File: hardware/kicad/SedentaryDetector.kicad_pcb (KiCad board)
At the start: 2 copper layers, 100 x 80 mm, 2 parts, among them J1 ESP32_2x15, J2 MPU6050_1x8

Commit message: feat(hardware): commit all hardware files for 100x80mm board
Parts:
- moved J2 47.7 mm to (149.5, 102.9)
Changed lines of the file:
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@@
 	(footprint ""
 		(layer "F.Cu")
-		(at 186.5 133)
+		(at 149.5 102.89)
 		(property "Reference" "J2"
 			(at 0 0 0)
@@
 		)
 		(property "Value" "MPU6050_1x8"
-			(at 0 0 0)
+			(at 6 3.38 0)
 			(layer "F.Fab")
 			(effects
@@
 		)
 		(property "Value" "ESP32_2x15"
-			(at 0 0 0)
+			(at 11 35.5 0)
 			(layer "F.Fab")
 			(effects
@@
 	)
 	(gr_text "J2-P8"
-		(at 188.5 115.22 0)
+		(at 151.5 85.34 0)
 		(layer "F.SilkS")
 		(effects
@@
 	)
 	(gr_text "J2-P7"
-		(at 188.5 117.76 0)
+		(at 151.5 87.88 0)
 		(layer "F.SilkS")
 		(effects
@@
 	)
 	(gr_text "J2-P6"
-		(at 188.5 120.3 0)
+		(at 151.5 90.42 0)
 		(layer "F.SilkS")
 		(effects
@@
 	)
 	(gr_text "J2-P5"
-		(at 188.5 122.84 0)
+		(at 151.5 92.96 0)
 		(layer "F.SilkS")
 		(effects
@@
 	)
 	(gr_text "J2-P4"
-		(at 188.5 125.38 0)
+		(at 151.5 95.5 0)
 		(layer "F.SilkS")
 		(effects
@@
 	)
 	(gr_text "J2-P3"
-		(at 188.5 127.92 0)
+		(at 151.5 98.04 0)
 		(layer "F.SilkS")
 		(effects
@@
 	)
 	(gr_text "J2-P2"
-		(at 188.5 130.46 0)
+		(at 151.5 100.58 0)
 		(layer "F.SilkS")
 		(effects
@@
 	)
 	(gr_text "J2-P1"
-		(at 188.5 133 0)
-		(layer "F.SilkS")
-		(effects
+		(at 151.5 103.12 0)
+		(layer "F.SilkS")
+		(effects

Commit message: chore: update PCB and scripts
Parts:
- moved J2 1.50 mm to (148.0, 103.0)
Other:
- board outline removed
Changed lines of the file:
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@@
 		(capping no)
 		(filling no)
+		(grid_origin 135.5 145)
 		(pcbplotparams
 			(layerselection 0x00000000_00000000_55555555_5755f5ff)
@@
 	(footprint ""
 		(layer "F.Cu")
-		(at 149.5 102.89)
+		(at 148 103)
 		(property "Reference" "J2"
 			(at 0 0 0)
@@
 		(embedded_fonts no)
 	)
-	(gr_line
-		(start 98.5 65)
-		(end 198.5 65)
-		(stroke
-			(width 0.1)
-			(type default)
-		)
-		(layer "Edge.Cuts")
-	)
-	(gr_line
-		(start 98.5 145)
-		(end 98.5 65)
-		(stroke
-			(width 0.1)
-			(type default)
-		)
-		(layer "Edge.Cuts")
-	)
-	(gr_line
-		(start 198.5 65)
-		(end 198.5 145)
-		(stroke
-			(width 0.1)
-			(type default)
-		)
-		(layer "Edge.Cuts")
-	)
-	(gr_line
-		(start 198.5 145)
-		(end 98.5 145)
-		(stroke
-			(width 0.1)
-			(type default)
-		)
-		(layer "Edge.Cuts")
-	)
 	(gr_text "L-P1"

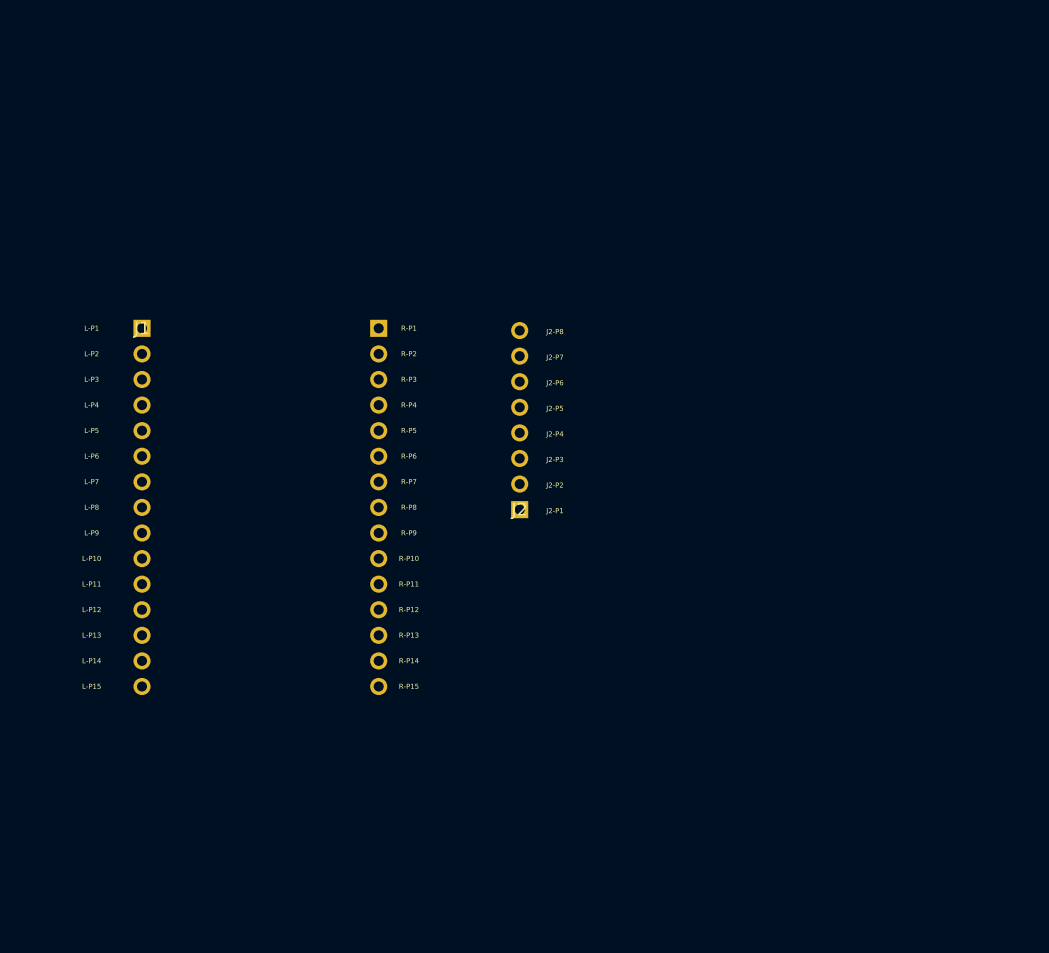
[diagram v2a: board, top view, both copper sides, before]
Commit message: fix(hardware): add missing Edge.Cuts board outline (100x80mm)
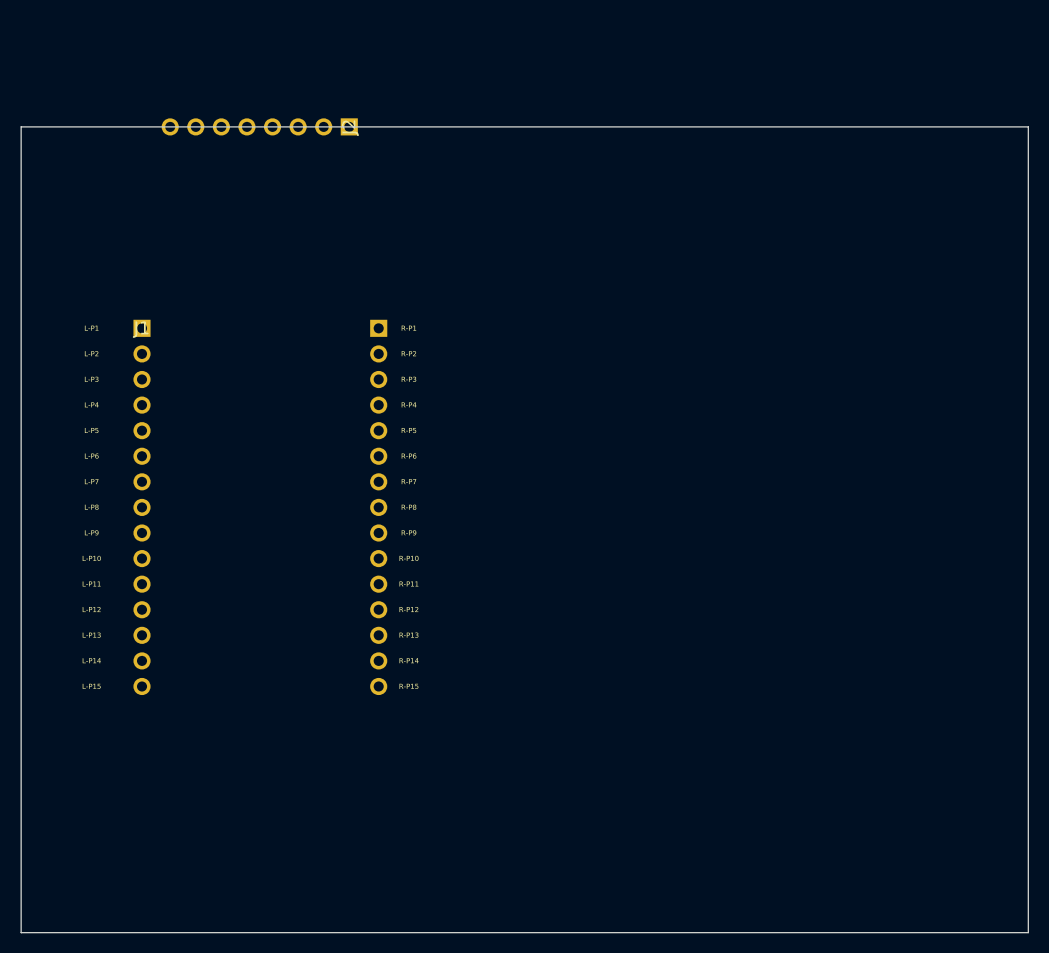
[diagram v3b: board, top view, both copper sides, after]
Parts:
- moved J2 41.6 mm to (131.1, 65.0), turned to 90 degrees
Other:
- board outline added: 100 x 80 mm
- board text removed: "J2-P1"
- board text removed: "J2-P2"
- board text removed: "J2-P3"
- board text removed: "J2-P4"
- board text removed: "J2-P5"
- board text removed: "J2-P6"
- board text removed: "J2-P7"
- board text removed: "J2-P8"
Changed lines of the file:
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@@
 	(footprint ""
 		(layer "F.Cu")
-		(at 148 103)
+		(at 131.08 65 90)
 		(property "Reference" "J2"
-			(at 0 0 0)
+			(at 0 0 90)
 			(layer "F.SilkS")
 			(effects
@@
 		)
 		(property "Value" "MPU6050_1x8"
-			(at 6 3.38 0)
+			(at 5.42 -8.5 0)
 			(layer "F.Fab")
 			(effects
@@
 		)
 		(property "Datasheet" ""
-			(at 0 0 0)
+			(at 0 0 90)
 			(layer "F.Fab")
 			(hide yes)
@@
 		)
 		(property "Description" ""
-			(at 0 0 0)
+			(at 0 0 90)
 			(layer "F.Fab")
 			(hide yes)
@@
 		(duplicate_pad_numbers_are_jumpers no)
 		(pad "1" thru_hole rect
-			(at 0 0)
+			(at 0 0 90)
 			(size 1.7 1.7)
 			(drill 1)
@@
 		)
 		(pad "2" thru_hole circle
-			(at 0 -2.54)
+			(at 0 -2.54 90)
 			(size 1.7 1.7)
 			(drill 1)
@@
 		)
 		(pad "3" thru_hole circle
-			(at 0 -5.08)
+			(at 0 -5.08 90)
 			(size 1.7 1.7)
 			(drill 1)
@@
 		)
 		(pad "4" thru_hole circle
-			(at 0 -7.62)
+			(at 0 -7.62 90)
 			(size 1.7 1.7)
 			(drill 1)
@@
 		)
 		(pad "5" thru_hole circle
-			(at 0 -10.16)
+			(at 0 -10.16 90)
 			(size 1.7 1.7)
 			(drill 1)
@@
 		)
 		(pad "6" thru_hole circle
-			(at 0 -12.7)
+			(at 0 -12.7 90)
 			(size 1.7 1.7)
 			(drill 1)
@@
 		)
 		(pad "7" thru_hole circle
-			(at 0 -15.24)
+			(at 0 -15.24 90)
 			(size 1.7 1.7)
 			(drill 1)
@@
 		)
 		(pad "8" thru_hole circle
-			(at 0 -17.78)
+			(at 0 -17.78 90)
 			(size 1.7 1.7)
 			(drill 1)
@@
 		(embedded_fonts no)
 	)
+	(gr_line
+		(start 98.5 65)
+		(end 198.5 65)
+		(stroke
+			(width 0.1)
+			(type default)
+		)
+		(layer "Edge.Cuts")
+	)
+	(gr_line
+		(start 98.5 145)
+		(end 98.5 65)
+		(stroke
+			(width 0.1)
+			(type default)
+		)
+		(layer "Edge.Cuts")
+	)
+	(gr_line
+		(start 198.5 65)
+		(end 198.5 145)
+		(stroke
+			(width 0.1)
+			(type default)
+		)
+		(layer "Edge.Cuts")
+	)
+	(gr_line
+		(start 198.5 145)
+		(end 98.5 145)
+		(stroke
+			(width 0.1)
+			(type default)
+		)
+		(layer "Edge.Cuts")
+	)
 	(gr_text "L-P1"
 		(at 105.5 85 0)
@@
 		(layer "F.SilkS")
 		(effects
-			(font
-				(size 0.5 0.5)
-				(thickness 0.15)
-			)
-		)
-	)
-	(gr_text "J2-P8"
-		(at 151.5 85.34 0)
-		(layer "F.SilkS")
-		(effects
-			(font
-				(size 0.5 0.5)
-				(thickness 0.15)
-			)
-		)
-	)
-	(gr_text "J2-P7"
-		(at 151.5 87.88 0)
-		(layer "F.SilkS")
-		(effects
-			(font
-				(size 0.5 0.5)
-				(thickness 0.15)
-			)
-		)
-	)
-	(gr_text "J2-P6"
-		(at 151.5 90.42 0)
-		(layer "F.SilkS")
-		(effects
-			(font
-				(size 0.5 0.5)
-				(thickness 0.15)
-			)
-		)
-	)
-	(gr_text "J2-P5"
-		(at 151.5 92.96 0)
-		(layer "F.SilkS")
-		(effects
-			(font
-				(size 0.5 0.5)
-				(thickness 0.15)
-			)
-		)
-	)
-	(gr_text "J2-P4"
-		(at 151.5 95.5 0)
-		(layer "F.SilkS")
-		(effects
-			(font
-				(size 0.5 0.5)
-				(thickness 0.15)
-			)
-		)
-	)
-	(gr_text "J2-P3"
-		(at 151.5 98.04 0)
-		(layer "F.SilkS")
-		(effects
-			(font
-				(size 0.5 0.5)
-				(thickness 0.15)
-			)
-		)
-	)
-	(gr_text "J2-P2"
-		(at 151.5 100.58 0)
-		(layer "F.SilkS")
-		(effects
-			(font
-				(size 0.5 0.5)
-				(thickness 0.15)
-			)
-		)
-	)
-	(gr_text "J2-P1"
-		(at 151.5 103.12 0)
-		(layer "F.SilkS")
-		(effects

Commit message: docs: add control circuit wiring table (ESP32 ↔ MPU6050)
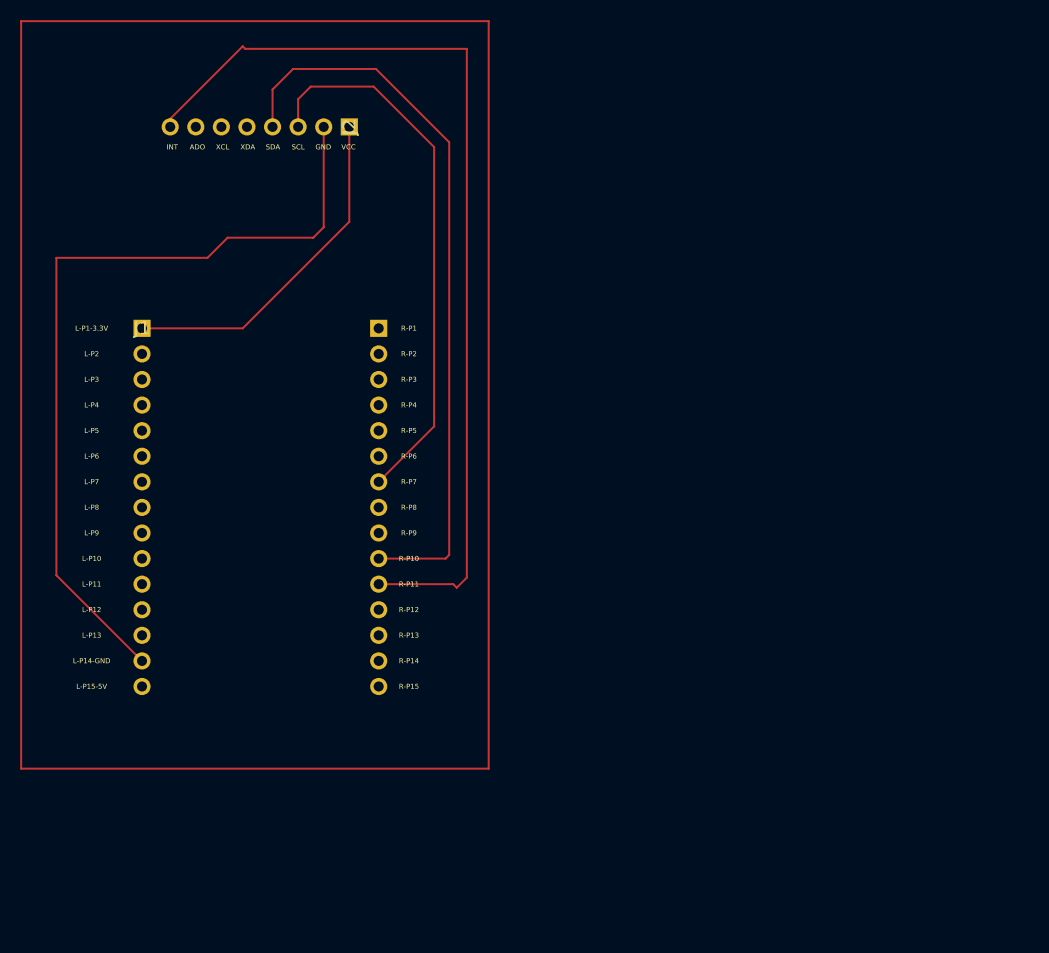
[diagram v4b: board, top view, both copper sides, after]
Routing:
- net (no net): track 0.00 -> 338.8 mm
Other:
- board outline removed
- board text added: "ADO"
- board text added: "GND"
- board text added: "INT"
- board text added: "L-P1-3.3V"
- board text added: "L-P14-GND"
- board text added: "L-P15-5V"
- board text added: "SCL"
- board text added: "SDA"
- board text added: "VCC"
- board text added: "XCL"
- board text added: "XDA"
- board text removed: "L-P1"
- board text removed: "L-P14"
- board text removed: "L-P15"
